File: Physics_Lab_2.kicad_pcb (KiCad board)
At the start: 2 copper layers, 54.5 x 66.6 mm, 9 parts, among them J1 USB_C, U1 MCP73871, U2 S2B-PH-K-S-GW

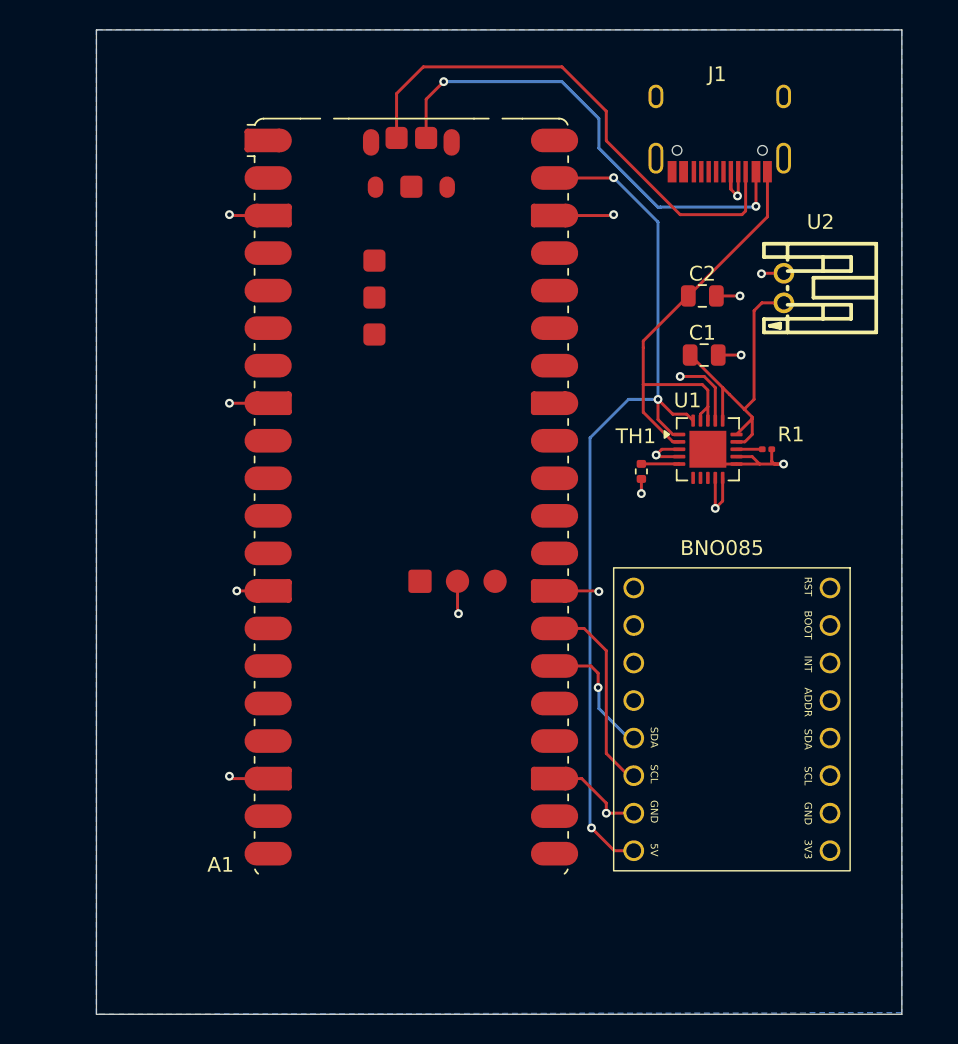
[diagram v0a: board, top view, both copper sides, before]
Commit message: Rearrange PCB design
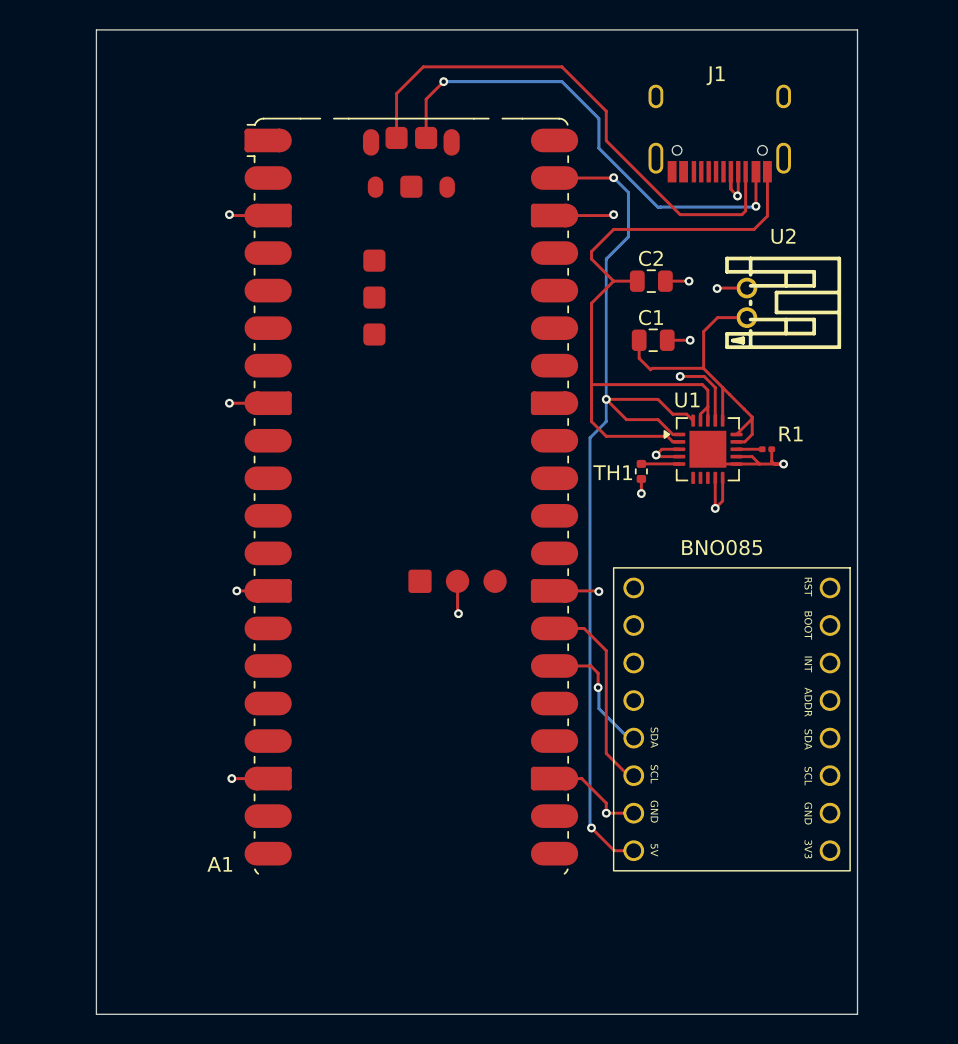
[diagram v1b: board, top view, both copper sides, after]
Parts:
- moved C1 3.59 mm to (144.2, 80.5)
- moved C2 3.59 mm to (144.1, 76.5)
- moved U2 2.69 mm to (150.5, 78.0)
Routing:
- net Net-(J1-VBUS): track 30.8 -> 48.0 mm
- net Net-(A1-VSYS): track 62.1 -> 65.4 mm
- net Net-(U1-V_{BAT_SENSE}): track 21.3 -> 22.6 mm
- removed copper zone on B.Cu, net GND
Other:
- board size 54.5 x 66.6 mm -> 51.5 x 66.6 mm

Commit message: Rearrange PCB design
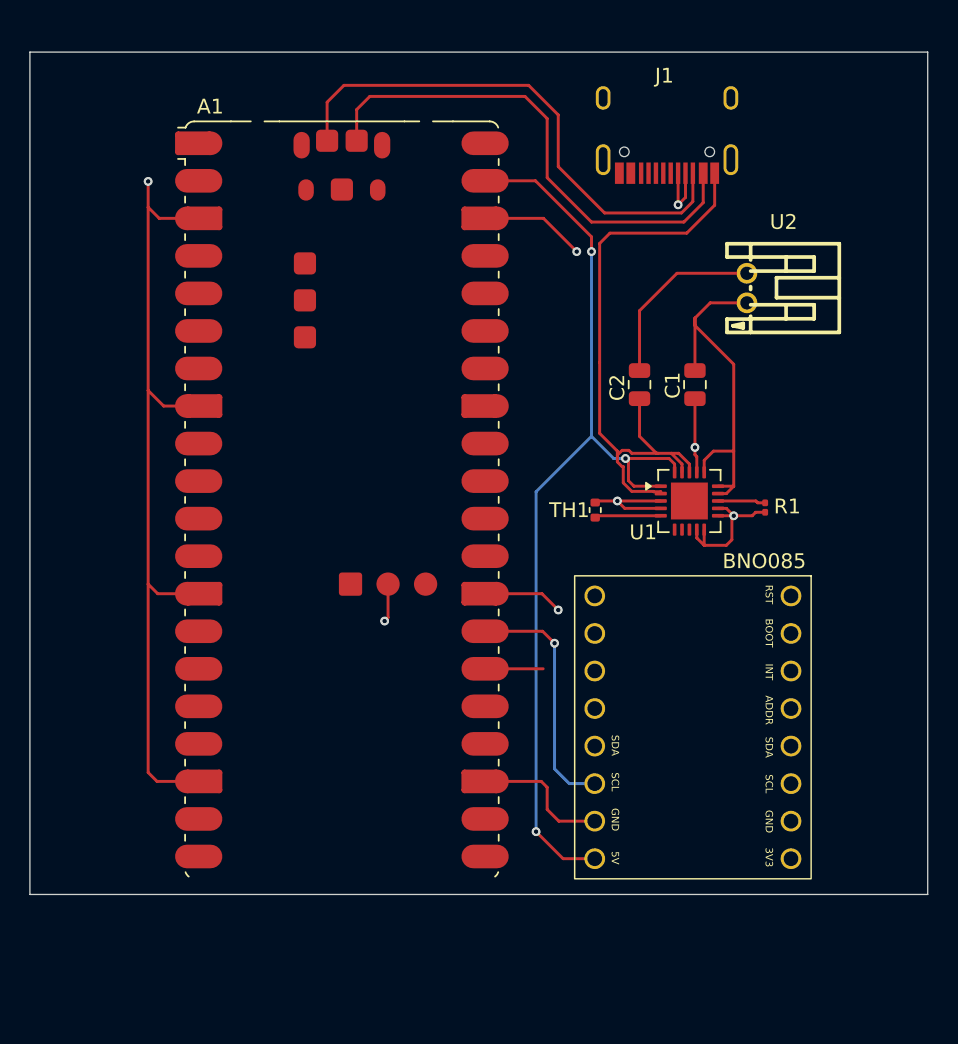
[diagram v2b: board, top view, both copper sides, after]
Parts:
- moved C2 7.05 mm to (143.2, 83.5), turned to -90 degrees
- moved A1 4.70 mm to (123.1, 91.3)
- moved C1 4.12 mm to (147.0, 83.5), turned to -90 degrees
- moved TH1 4.07 mm to (140.2, 92.0), turned to -90 degrees
- moved R1 3.95 mm to (151.8, 91.8), turned to 90 degrees
- moved U1 3.72 mm to (146.6, 91.4)
- moved J1 3.57 mm to (145.1, 61.5)
- moved BNO085_Halley1 2.69 mm to (153.5, 97.8)
- moved U2 1.00 mm to (150.5, 77.0)
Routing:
- net GND: track 57.9 -> 119.9 mm, vias 17 -> 8
- net Net-(J1-VBUS): track 48.0 -> 42.7 mm
- net Net-(A1-GPIO20): track 8.39 -> 4.20 mm, vias 1 -> 0
- net Net-(A1-GPIO21): track 13.2 -> 16.9 mm, vias 0 -> 1
- net Net-(U1-V_{BAT_SENSE}): track 22.6 -> 25.4 mm
- net Net-(U1-THERM): track 2.57 -> 4.49 mm
- net Net-(A1-USB_DM): track 32.5 -> 34.3 mm, vias 2 -> 0
- net Net-(U1-PROG1): track 1.74 -> 3.24 mm
- net Net-(A1-VSYS): track 65.4 -> 66.5 mm
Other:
- board size 51.5 x 66.6 mm -> 60.8 x 57 mm
